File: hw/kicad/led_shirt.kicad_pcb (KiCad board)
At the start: 2 copper layers, 0 parts

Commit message: rev 2 board done
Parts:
- added C1: 4.7µF, SM0603, F.Cu at (143.0, 94.5)
- added C2: 4.7µF, SM0603, F.Cu at (143.9, 104.3)
- added D1: LED, SM0603, F.Cu at (140.6, 93.5)
- added J1: 10103593-0001LF, 10118193-0001LF, F.Cu at (141.0, 99.1)
- added P1: c, test_pad_smd, F.Cu at (144.0, 107.7)
- added P2: d, test_pad_smd, F.Cu at (142.7, 107.7)
- added P3: g, test_pad_smd, F.Cu at (141.5, 107.7)
- added P4: v, test_pad_smd, F.Cu at (140.2, 107.7)
- added P5: m, test_pad_smd, F.Cu at (138.9, 107.7)
- added P6: bat+, noah_hole_1, F.Cu at (156.2, 104.3)
- added P7: bat-, noah_hole_1, F.Cu at (156.2, 106.8)
- added P8: led1-, noah_hole_1, F.Cu at (156.2, 97.8)
- added P9: led1+, noah_hole_1, F.Cu at (156.2, 100.3)
- added Q1: MOS_N_np, SOT23, F.Cu at (152.3, 93.0)
- added R1: 3.3kΩ, SM0603, F.Cu at (142.4, 91.7)
- added R2: 3.3kΩ, SM0603, F.Cu at (147.2, 95.0)
- added R3: 10kΩ, SM0603, F.Cu at (141.7, 104.8)
- added R4: 0Ω, SM0603, F.Cu at (156.1, 93.5)
- added SW1: SW_PUSH, SW_PB_4PIN_SMT_real, F.Cu at (149.1, 99.1)
- added U1: MCP73831, MCP73831, F.Cu at (145.0, 91.7)
- added U2: PIC12F1822, PIC12F1822-SOIC-8, F.Cu at (146.3, 103.6)
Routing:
- net vbat: track 0.00 -> 33.8 mm, vias 0 -> 2
- net N-0000015: track 0.00 -> 28.1 mm, vias 0 -> 4
- net vbus: track 0.00 -> 20.6 mm, vias 0 -> 3
- net N-0000010: track 0.00 -> 15.1 mm
- net icspdat: track 0.00 -> 13.8 mm, vias 0 -> 2
- net icspclk: track 0.00 -> 11.2 mm, vias 0 -> 2
- net mclr: track 0.00 -> 10.3 mm, vias 0 -> 2
- net GND: track 0.00 -> 7.74 mm, vias 0 -> 2
- net N-000007: track 0.00 -> 5.15 mm
- net N-0000016: track 0.00 -> 4.16 mm
- net N-0000017: track 0.00 -> 3.61 mm
- net N-000002: track 0.00 -> 1.91 mm
- net N-000003: track 0.00 -> 1.88 mm
- added copper zone on B.Cu, net GND
- added copper zone on F.Cu, net GND
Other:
- board outline added: 21.7 x 18.9 mm
- board text added: "led_shirt github.com/noahp/ledshirt v2.0 oct-2013"

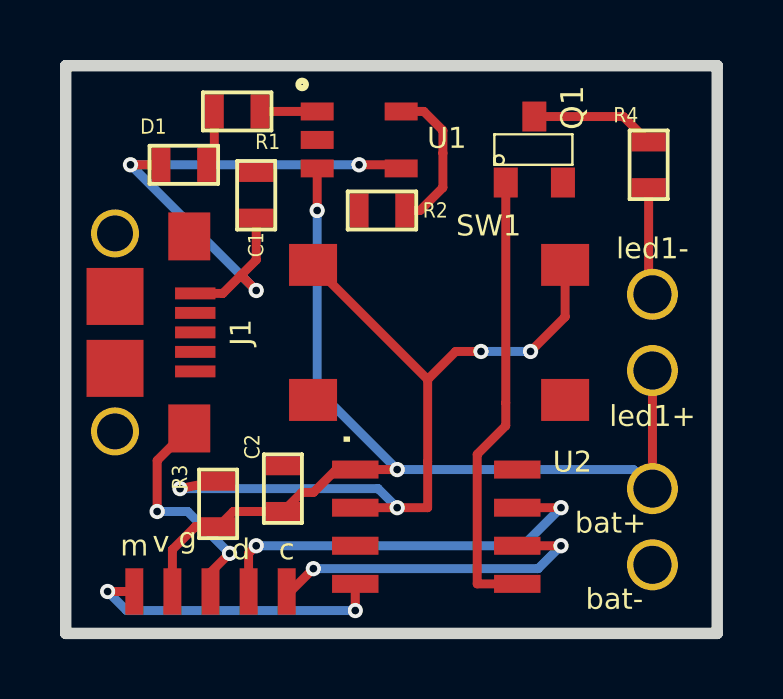
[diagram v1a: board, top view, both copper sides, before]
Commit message: - update pcb & gerbers with new pullups
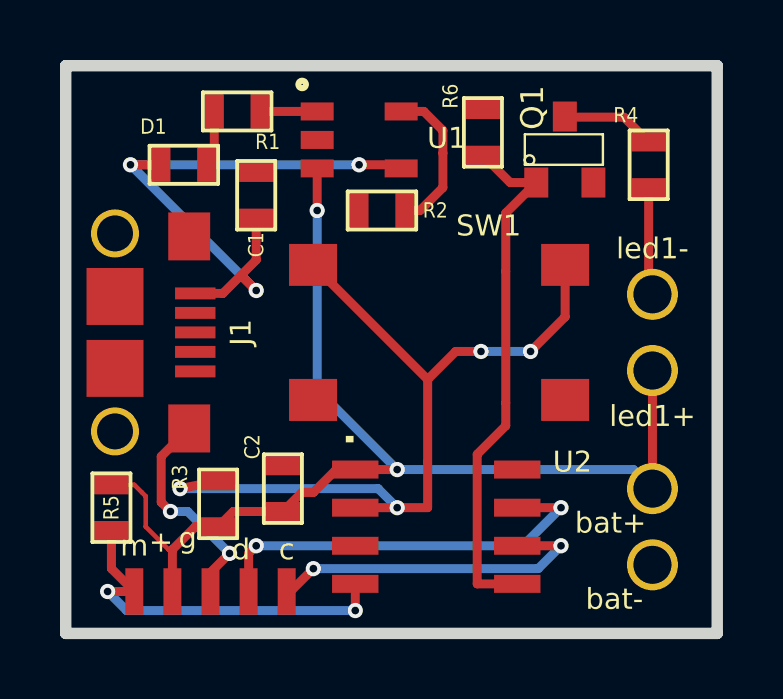
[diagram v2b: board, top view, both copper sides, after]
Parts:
- added R5: 10K, SM0603, F.Cu at (138.2, 104.9)
- added R6: 10K, SM0603, F.Cu at (150.6, 92.4)
- P4: value v -> +
- moved Q1 1.02 mm to (153.3, 93.0)
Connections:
- J1 pad 2: N-0000013 -> (no net)
- J1 pad 3: N-0000012 (its old number) -> (no net)
- J1 pad 4: N-0000011 (its old number) -> (no net)
- U2 pad 3: N-000009 (its old number) -> (no net)
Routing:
- net vbat: track 33.8 -> 37.4 mm
- net N-000006: track 15.1 -> 17.7 mm
- net mclr: track 10.3 -> 12.6 mm
- net N-000008: track 4.16 -> 3.14 mm

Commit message: - start layout
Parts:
- removed P8: led1-, noah_hole_1
- removed P9: led1+, noah_hole_1
- added D2: LED, plcc2, F.Cu at (160.7, 103.5)
- added D3: LED, plcc2, F.Cu at (160.7, 89.5)
- added D4: LED, plcc2, F.Cu at (146.7, 89.5)
- added D5: LED, plcc2, F.Cu at (146.7, 103.5)
- P1: value c -> icpc
- P2: value d -> icpd
- P3: value g -> gnd
- P4: value + -> v+
- P5: value m -> mclr
- moved D1 34.9 mm to (175.3, 97.8)
- moved P6 33.9 mm to (128.3, 85.1)
- moved P7 31.1 mm to (134.0, 85.1)
- moved C1 21.5 mm to (160.0, 81.3), turned to 0 degrees
- moved R2 21.1 mm to (165.1, 83.8), turned to 0 degrees
- moved Q1 20.9 mm to (135.3, 103.5)
- moved R4 20.3 mm to (139.7, 105.4), turned to 0 degrees
- moved P5 18.8 mm to (123.8, 96.5)
- moved P4 17.8 mm to (126.4, 96.5)
- moved R1 17.0 mm to (158.2, 97.8)
- moved P3 16.8 mm to (128.9, 96.5)
- moved P2 15.9 mm to (131.4, 96.5)
- moved P1 15.0 mm to (134.0, 96.5)
- moved R6 14.6 mm to (145.4, 106.0), turned to 0 degrees
- moved U1 10.9 mm to (155.6, 88.9), turned to 90 degrees
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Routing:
- net vbat: track 37.4 -> 0.00 mm, vias 2 -> 0
- net N-000007: track 28.1 -> 0.00 mm, vias 4 -> 0
- net vbus: track 20.6 -> 0.00 mm, vias 3 -> 0
- net N-0000013: track 17.7 -> 0.00 mm
- net icspdat: track 13.8 -> 0.00 mm, vias 2 -> 0
- net mclr: track 12.6 -> 0.00 mm, vias 2 -> 0
- net icspclk: track 11.2 -> 0.00 mm, vias 2 -> 0
- net GND: track 7.36 -> 0.00 mm, vias 2 -> 0
- net N-000004: track 5.15 -> 0.00 mm
- net N-000006: track 3.61 -> 0.00 mm
- net N-0000011: track 3.14 -> 0.00 mm
- net N-000001: track 1.91 -> 0.00 mm
- net N-000003: track 1.88 -> 0.00 mm
- removed copper zone on B.Cu, net GND
- removed copper zone on F.Cu, net GND
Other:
- board size 21.7 x 18.9 mm -> 24.7 x 24.7 mm

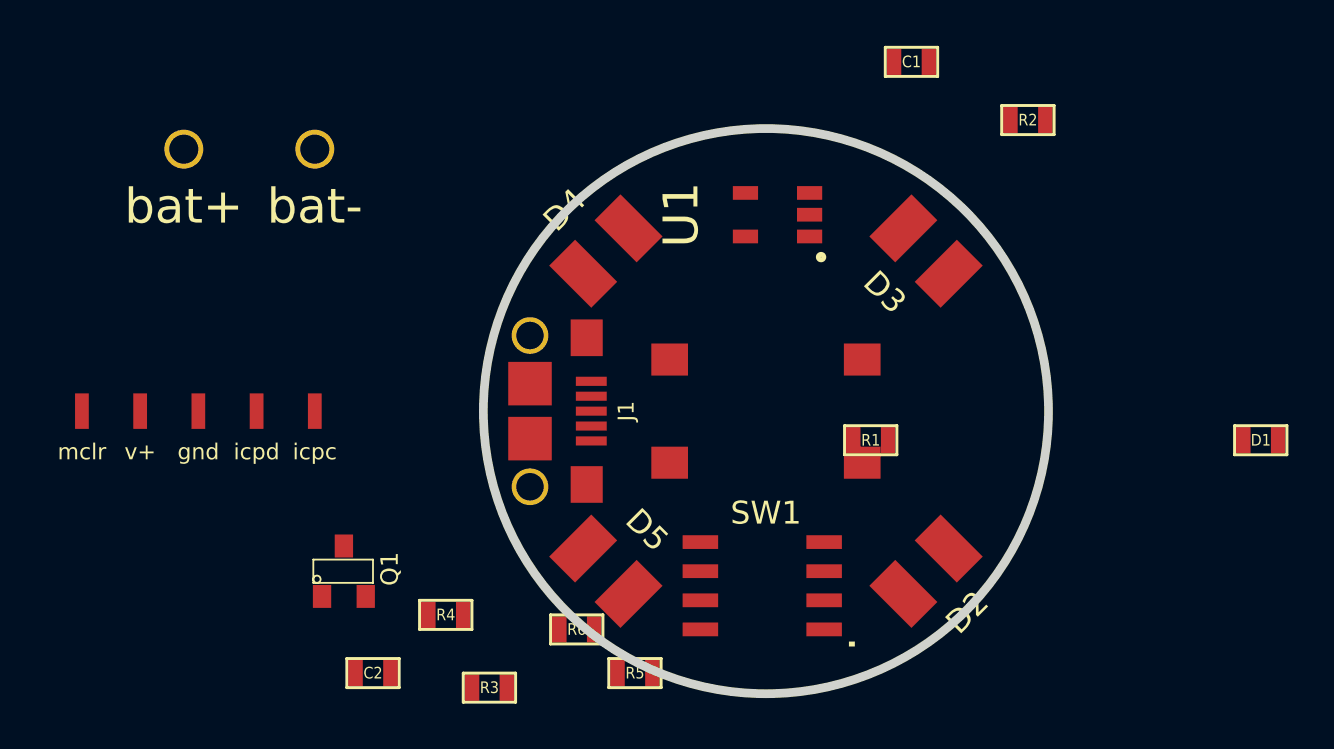
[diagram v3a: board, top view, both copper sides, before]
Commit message: - two sides! also delete programming pins, who needs 'em
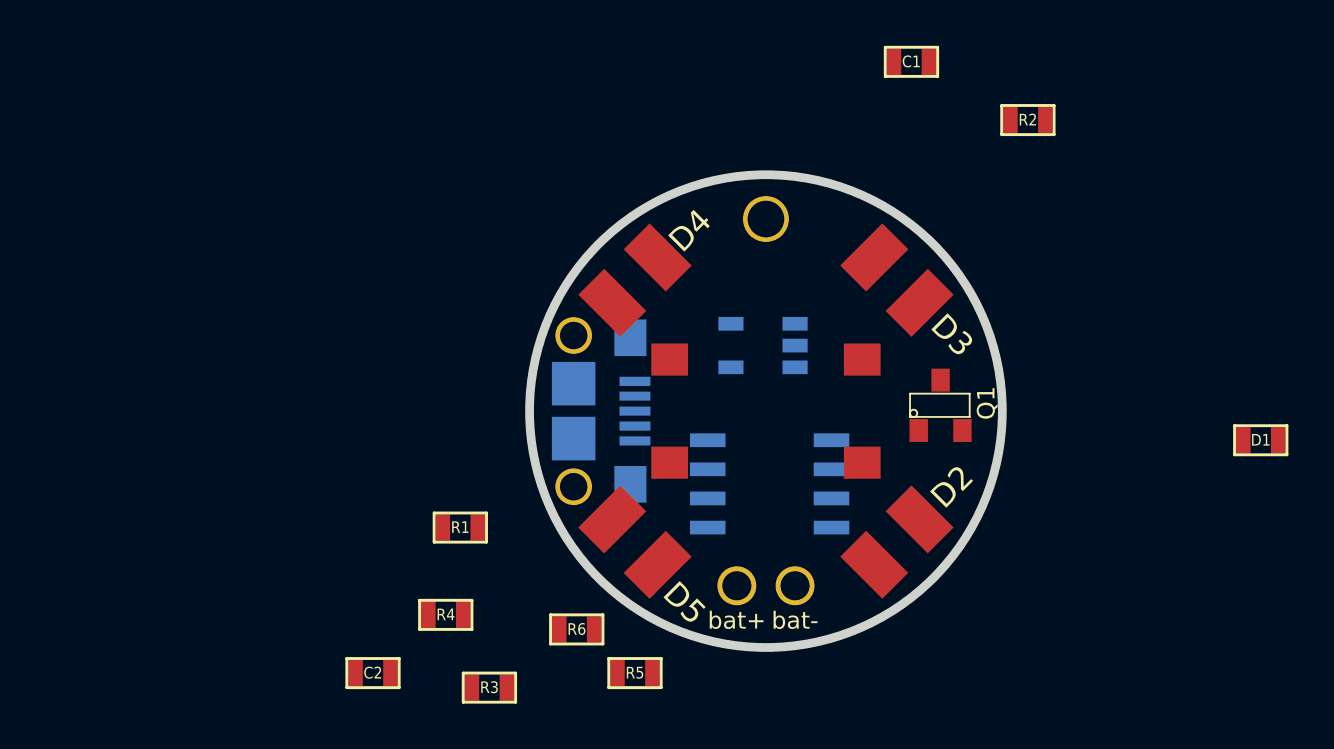
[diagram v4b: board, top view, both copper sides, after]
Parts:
- removed P1: icpc, test_pad_smd
- removed P2: icpd, test_pad_smd
- removed P3: gnd, test_pad_smd
- removed P4: v+, test_pad_smd
- removed P5: mclr, test_pad_smd
- added med_test_hole: VAL**, med_test_hole, F.Cu at (153.7, 88.1)
- J1, U1, U2: moved to B.Cu
- moved P6 30.7 mm to (152.4, 104.1)
- moved P7 28.3 mm to (154.9, 104.1)
- moved Q1 27.0 mm to (161.3, 96.3)
- moved R1 18.3 mm to (140.3, 101.6)
- moved U2 6.75 mm to (151.1, 101.6)
- moved U1 3.86 mm to (154.9, 92.7), turned to 270 degrees
- moved J1 1.91 mm to (148.0, 96.5), turned to 90 degrees
- moved D3 1.80 mm to (159.4, 90.8)
- moved D4 1.80 mm to (148.0, 90.8)
- moved D2 1.80 mm to (159.4, 102.2)
- moved D5 1.80 mm to (148.0, 102.2)
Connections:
- U2 pad 6: icspclk -> (no net)
- U2 pad 7: icspdat -> (no net)
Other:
- board size 24.7 x 24.7 mm -> 20.6 x 20.6 mm
- board text added: "+"
- board text added: "-"
- board text added: "c"
- board text added: "d"
- board text added: "m"

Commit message: work on pcb
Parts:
- added med_test_hole: VAL**, med_test_hole, F.Cu at (155.7, 88.1)
- C1, D1, R1, R2, R4: moved to B.Cu
- P6: value bat+ -> b+
- P7: value bat- -> b-
- moved C2 23.6 mm to (156.5, 95.2), turned to 90 degrees
- moved D1 22.2 mm to (154.2, 90.7)
- moved R4 21.5 mm to (158.5, 95.0)
- moved R1 19.8 mm to (157.2, 91.2), turned to 90 degrees
- moved R2 15.2 mm to (151.6, 90.9), turned to 270 degrees
- moved C1 14.5 mm to (149.6, 91.4), turned to 270 degrees
- moved R6 10.6 mm to (154.7, 100.8), turned to 270 degrees
- moved R5 8.52 mm to (152.7, 100.8), turned to 270 degrees
- moved med_test_hole 2.03 mm to (151.6, 88.1)
- moved U1 0.51 mm to (154.9, 93.2)

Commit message: new pcb
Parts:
- C2, R3: moved to B.Cu
- moved R3 9.35 mm to (148.6, 102.4), turned to 90 degrees
- moved C1 2.09 mm to (151.6, 90.9)
- moved R2 2.09 mm to (149.6, 91.4), turned to 90 degrees
- moved R4 1.93 mm to (159.3, 96.8), turned to 90 degrees
- moved C2 0.38 mm to (156.8, 95.2), turned to 270 degrees
- moved D1 0.25 mm to (154.2, 90.9), turned to 90 degrees
- turned D2 to 225 degrees
- turned D3 to 135 degrees
- turned R1 to 270 degrees
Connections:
- med_test_hole pad 1: (no net) -> GND (x2)
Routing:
- net vbat: track 0.00 -> 49.1 mm, vias 0 -> 1
- net N-0000018: track 0.00 -> 35.3 mm, vias 0 -> 2
- net GND: track 0.00 -> 15.3 mm, vias 0 -> 2
- net vbus: track 0.00 -> 13.0 mm
- net N-0000011: track 0.00 -> 7.94 mm, vias 0 -> 2
- net N-0000017: track 0.00 -> 4.94 mm, vias 0 -> 1
- net mclr: track 0.00 -> 3.55 mm, vias 0 -> 1
- net N-0000013: track 0.00 -> 3.15 mm
- net N-0000014: track 0.00 -> 2.96 mm
- net N-000001: track 0.00 -> 2.81 mm
- net N-0000016: track 0.00 -> 2.38 mm, vias 0 -> 1
- added copper zone on B.Cu, net GND
- added copper zone on F.Cu, net GND
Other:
- board text added: "git.io/FEFjUw v2.0"
- board text added: "ledshirt"
- board text removed: "led_shirt github.com/noahp/ledshirt v2.0 oct-2013"
